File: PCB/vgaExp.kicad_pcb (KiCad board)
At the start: 2 copper layers, 80 x 91.1 mm, 83 parts, among them J1 DE-15, J2 DE-15, J3 VHDCI, P5 CONN_1, P6 CONN_1, P7 CONN_6, U1 ADP3303-3V3, U2 ADP3334, U3 AD9984, U4 ADP3334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

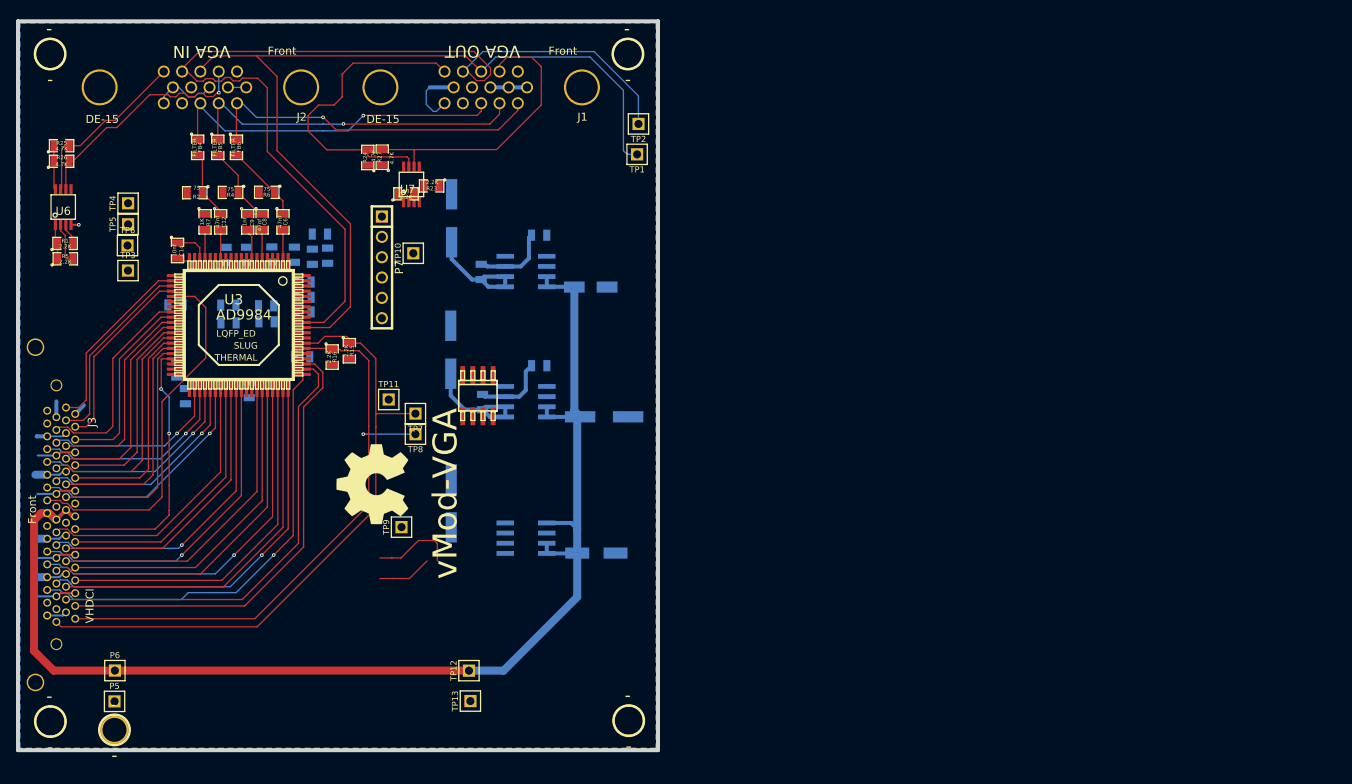
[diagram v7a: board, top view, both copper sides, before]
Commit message: Routing complete. Also Fixes #6
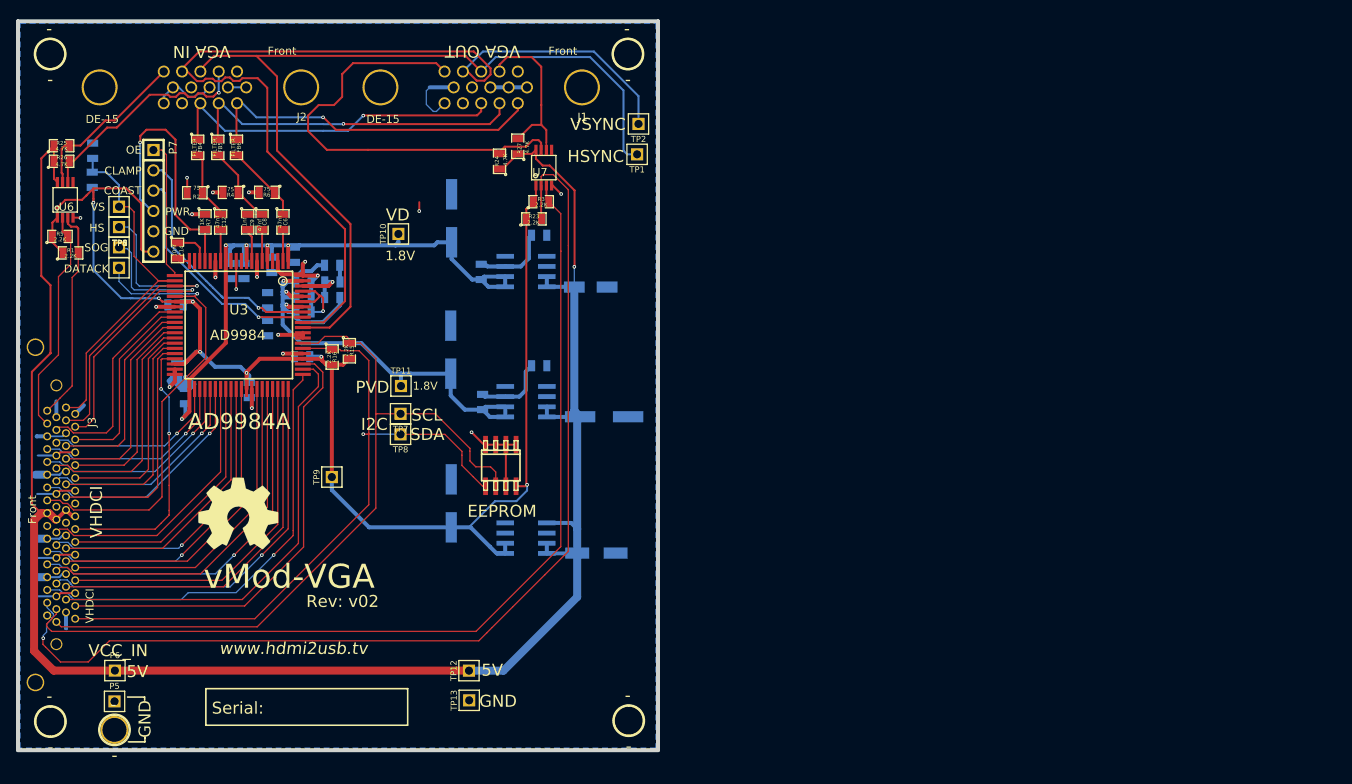
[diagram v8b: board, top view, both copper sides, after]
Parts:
- moved P7 29.7 mm to (104.8, 40.7)
- moved R10 27.4 mm to (97.2, 34.4), turned to 270 degrees
- moved R9 23.1 mm to (97.2, 38.0), turned to 90 degrees
- moved l1 17.2 mm to (115.4, 79.8), turned to 0 degrees
- moved R27 17.0 mm to (150.4, 33.9)
- moved R3 16.9 mm to (153.3, 40.8)
- moved U7 16.7 mm to (153.6, 36.5)
- moved R24 16.5 mm to (148.1, 35.7)
- moved R23 13.4 mm to (152.4, 42.9), turned to 0 degrees
- moved TP9 10.7 mm to (127.1, 75.2)
- moved U5 9.18 mm to (148.2, 73.8)
- moved R8 6.18 mm to (127.2, 50.8)
- moved C15 5.68 mm to (127.2, 52.8), turned to 180 degrees
- moved TP10 3.05 mm to (135.4, 44.8)
- moved R5 2.88 mm to (93.2, 45.1)
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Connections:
- J3 pad 35: /I2C/DDC Section/SCL_VGA_RX_BUF -> /I2C/DDC Section/SDA_VGA_RX_BUF
- J3 pad 37: /I2C/DDC Section/SDA_VGA_RX_BUF -> /I2C/DDC Section/SCL_VGA_RX_BUF
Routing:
- net /I2C/DDC Section/OVDD: track 4.37 -> 187.6 mm, vias 0 -> 7
- net /I2C/DDC Section/SCL_VGA_TX_BUF: track 0.00 -> 133.2 mm, vias 0 -> 1
- net /I2C/DDC Section/SDA_VGA_TX_BUF: track 0.00 -> 117.5 mm
- net /I2C/DDC Section/GND: track 67.0 -> 141.8 mm, vias 1 -> 18
- net /I2C/DDC Section/VCC: track 159.8 -> 234.1 mm, vias 0 -> 1
- net /PowerSupply/VD: track 14.7 -> 85.8 mm, vias 0 -> 5
- net /PowerSupply/PVD: track 14.9 -> 72.9 mm, vias 0 -> 3
- net /CLAMP: track 0.00 -> 32.1 mm, vias 0 -> 1
- net /COST: track 0.00 -> 30.6 mm, vias 0 -> 1
- net /PWRDWN: track 3.94 -> 33.2 mm, vias 0 -> 1
- net /I2C/DDC Section/SDA_VGA_RX_BUF: track 2.69 -> 26.7 mm
- net /I2C/DDC Section/SCL_VGA_RX_BUF: track 5.29 -> 28.3 mm
- net /VSOUT: track 23.6 -> 46.1 mm
- net /HSOUT: track 24.8 -> 43.9 mm, vias 0 -> 1
- net /OE_Field: track 0.00 -> 17.4 mm
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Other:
- board text added: "1.8V"
- board text added: "5V"
- board text added: "AD9984A"
- board text added: "CLAMP"
- board text added: "COAST"
- board text added: "DATACK"
- board text added: "EEPROM"
- board text added: "GND"
- board text added: "HS"
- board text added: "HSYNC"
- board text added: "I2C"
- board text added: "OE"
- board text added: "PVD"
- board text added: "PWR"
- board text added: "Rev: v02"
- board text added: "SCL"
- board text added: "SDA"
- board text added: "SOG"
- board text added: "Serial:"
- board text added: "V.Reg: OVDD"
- board text added: "V.Reg: PD"
- board text added: "V.Reg: VD"
- board text added: "VCC_IN"
- board text added: "VD"
- board text added: "VHDCI"
- board text added: "VS"
- board text added: "VSYNC"
- board text added: "www.hdmi2usb.tv"
